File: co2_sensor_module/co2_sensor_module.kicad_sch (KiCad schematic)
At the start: 0 parts

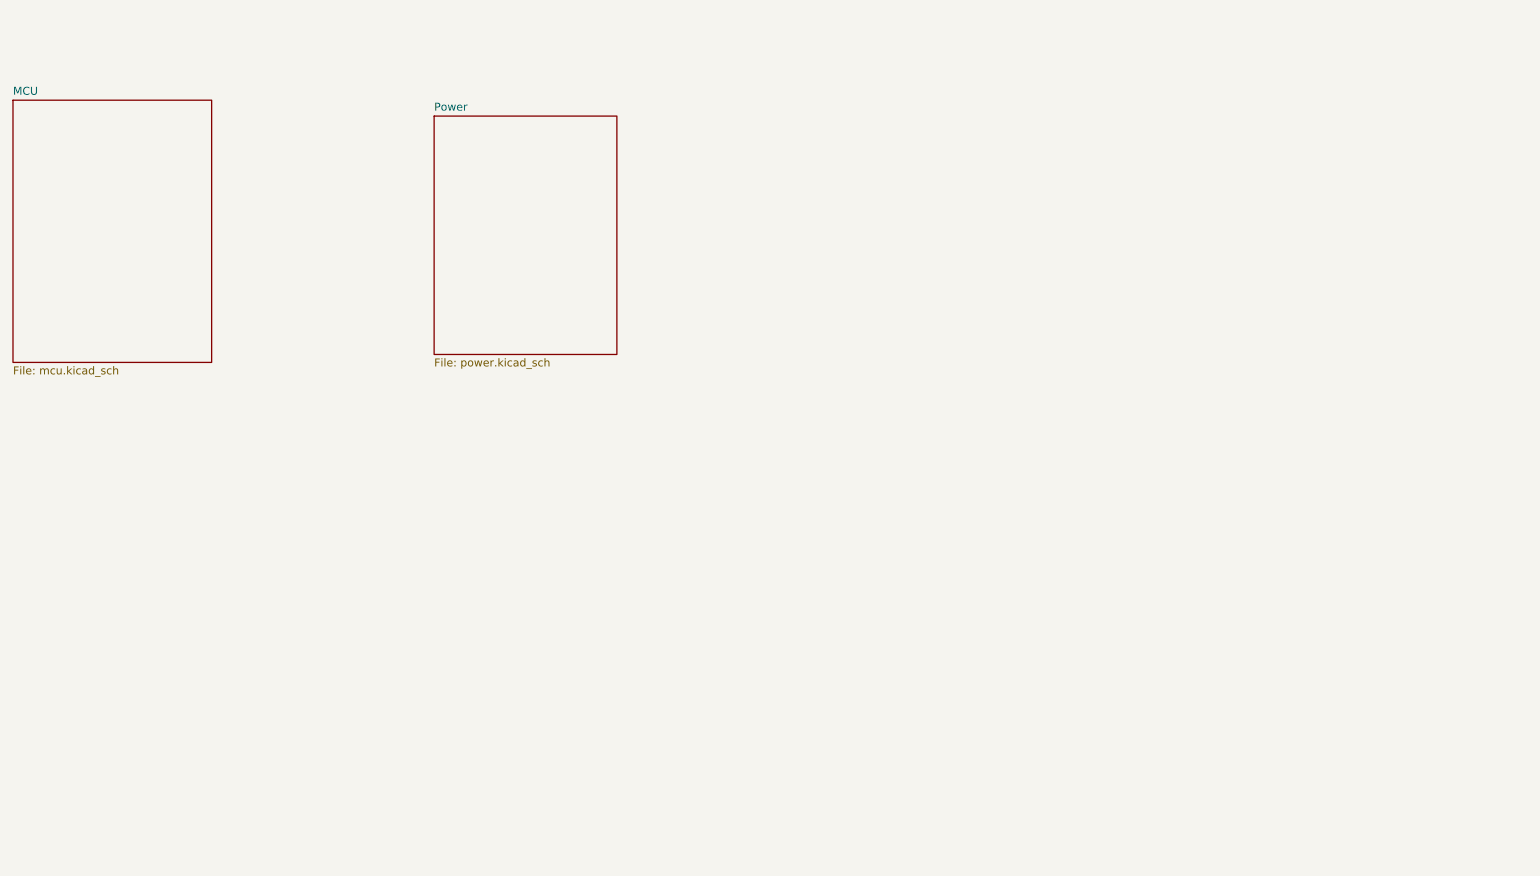
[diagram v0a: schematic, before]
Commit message: mostly done w/ sensor module
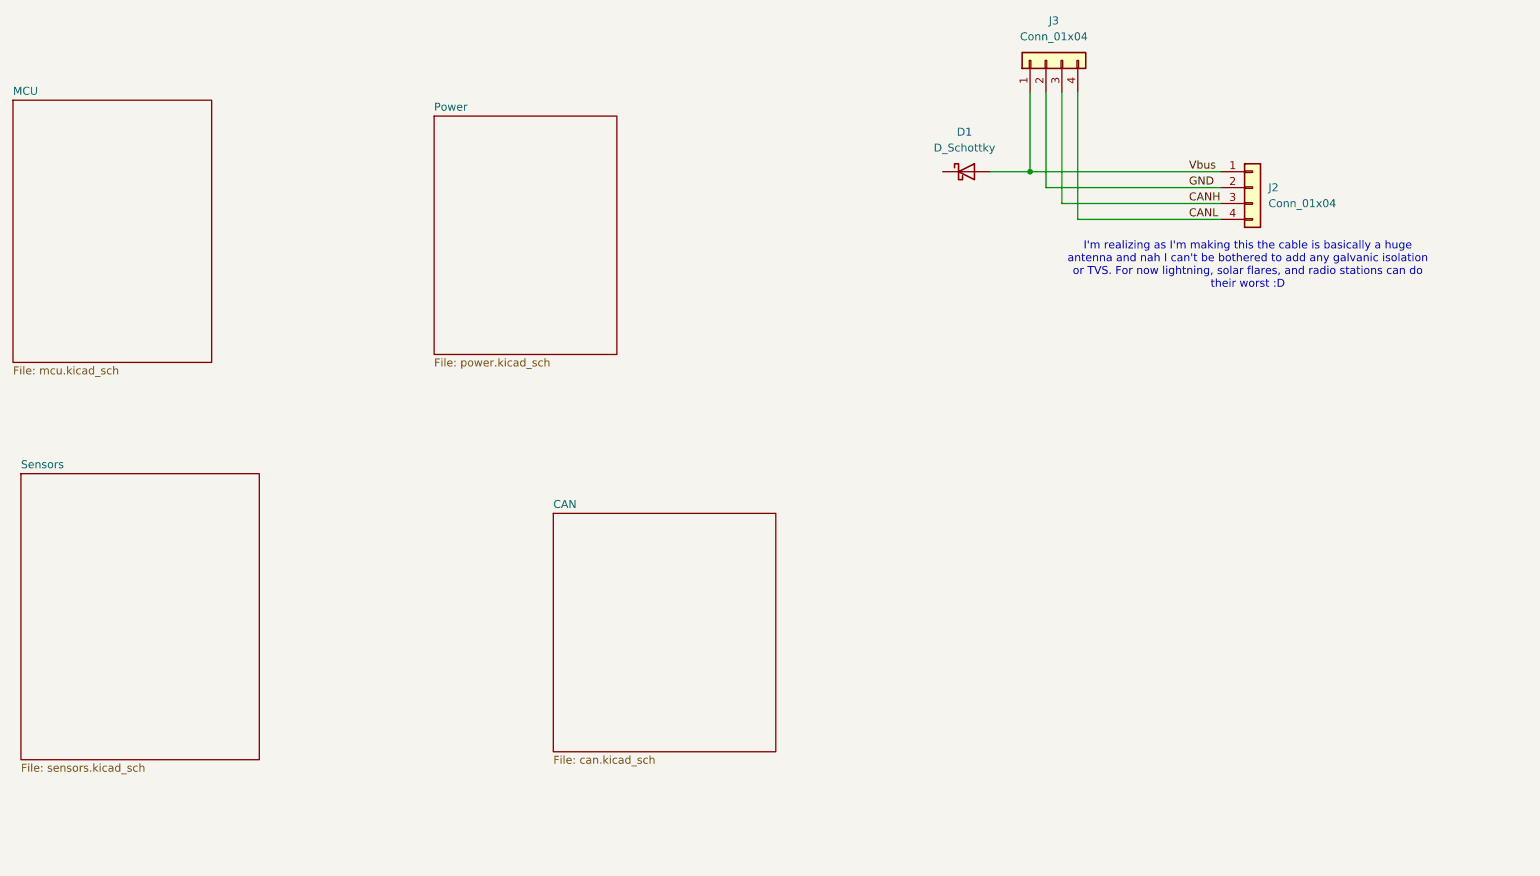
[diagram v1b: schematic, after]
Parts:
- added D1: D_Schottky, Diode_SMD:D_SOD-123, symbol Device:D_Schottky
- added J2, J3: Conn_01x04, symbol Connector_Generic:Conn_01x04
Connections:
- new net CANH: J2.3 (Pin_3), J3.3 (Pin_3)
- new net CANL: J2.4 (Pin_4), J3.4 (Pin_4)
- new net GND: J2.2 (Pin_2), J3.2 (Pin_2)
- new net Vbus: D1.2 (A), J2.1 (Pin_1), J3.1 (Pin_1)
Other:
- added sheet CAN (can.kicad_sch)
- added sheet Sensors (sensors.kicad_sch)
- note added: "I'm realizing as I'm making this the cable is basically a huge antenna and nah I can't be bothered to add any galvanic isolation or TVS. For now lightning, solar flares, and radio stations can do their worst :D"

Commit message: first draft of sensor schematic is done!
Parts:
- added J4: Conn_01x03, symbol Connector_Generic:Conn_01x03
- added J5: Conn_01x04, symbol Connector_Generic:Conn_01x04
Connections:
- net GND: now also J4.1 (Pin_1), J5.1 (Pin_1)
- net Power/Vbus: now reaches D1.1 (K)
- new net MCU/I2C_SCL: J5.4 (Pin_4)
- new net MCU/I2C_SDA: J5.3 (Pin_3)
- new net MCU/UART_RX: J4.2 (Pin_2)
- new net MCU/UART_TX: J4.3 (Pin_3)
- new net P3V3: J5.2 (Pin_2)
- no-connect marks 0 -> 1
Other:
- sheet CAN ports: added CANH, CANL, GND, P3V3, PV50, RX, STANDBY, TX; removed none
- sheet MCU ports: added CAN_RX, CAN_STANDBY, CAN_TX, GND, I2C_SCL, I2C_SDA, P3V3, UART_RX, UART_TX, ~{nRST}; removed none
- sheet Power ports: added GND, P3V3, P3V3_PGOOD, P5V0, P5V0_PGOOD, Vbus; removed none
- sheet Sensors ports: added GND, I2C_SCL, I2C_SDA, P3V3; removed none
- note added: "A UART header"
- note added: "An I2C expansion header"
- note added: "At least some reverse voltage protection would be useful"

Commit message: added wip hub + o2 sensor
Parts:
- J2, J3: footprint (none) -> Connector_JST:JST_PH_B4B-PH-K_1x04_P2.00mm_Vertical
- J4: footprint (none) -> Connector_PinHeader_2.54mm:PinHeader_1x03_P2.54mm_Vertical
- J5: footprint (none) -> Connector_PinHeader_2.54mm:PinHeader_1x04_P2.54mm_Vertical
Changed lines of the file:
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@@
 			)
 		)
-		(property "Footprint" ""
+		(property "Footprint" "Connector_PinHeader_2.54mm:PinHeader_1x04_P2.54mm_Vertical"
 			(at 106.68 140.97 0)
 			(hide yes)
@@
 			)
 		)
-		(property "Footprint" ""
+		(property "Footprint" "Connector_PinHeader_2.54mm:PinHeader_1x03_P2.54mm_Vertical"
 			(at 167.64 137.16 0)
 			(hide yes)
@@
 			)
 		)
-		(property "Footprint" ""
+		(property "Footprint" "Connector_JST:JST_PH_B4B-PH-K_1x04_P2.00mm_Vertical"
 			(at 215.9 38.1 0)
 			(hide yes)
@@
 			)
 		)
-		(property "Footprint" ""
+		(property "Footprint" "Connector_JST:JST_PH_B4B-PH-K_1x04_P2.00mm_Vertical"
 			(at 248.92 58.42 0)
 			(hide yes)

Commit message: some work on layout for co2 sensor unit
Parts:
- removed J5: Conn_01x04, Connector_PinHeader_2.54mm:PinHeader_1x04_P2.54mm_Vertical, symbol Connector_Generic:Conn_01x04
- added H1, H2, H3, H4: MountingHole 3M, MountingHole:MountingHole_3.2mm_M3, symbol Mechanical:MountingHole
- added J6, J7: Conn_01x05, Connector_PinHeader_2.54mm:PinHeader_1x05_P2.54mm_Vertical, symbol Connector_Generic:Conn_01x05
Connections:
- net GND: now also J6.1 (Pin_1), J7.1 (Pin_1)
- net MCU/I2C_SCL: now also J6.5 (Pin_5), J7.5 (Pin_5)
- net MCU/I2C_SDA: now also J6.4 (Pin_4), J7.4 (Pin_4)
- net P3V3: now also J6.2 (Pin_2), J7.2 (Pin_2)
- new net P5V0: J6.3 (Pin_3), J7.3 (Pin_3)
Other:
- note added: "Some I2C expansion headers"
- note removed: "An I2C expansion header"

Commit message: (mostly) finalized sensing units + progress on surface hub
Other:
- note removed: "I'm realizing as I'm making this the cable is basically a huge antenna and nah I can't be bothered to add any galvanic isolation or TVS. For now lightning, solar flares, and radio stations can do their worst :D"
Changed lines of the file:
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@@
-		)
-	)
-	(text "I'm realizing as I'm making this the cable is basically a huge\nantenna and nah I can't be bothered to add any galvanic isolation\nor TVS. For now lightning, solar flares, and radio stations can do\ntheir worst :D"
-		(exclude_from_sim no)
-		(at 252.984 70.358 0)
-		(effects
-			(font
-				(size 1.27 1.27)
-			)
 		)
 	)

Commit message: progress on solar charging + misc
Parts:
- D1: value D_Schottky -> B5819W Schottky
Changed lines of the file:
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@@
 			)
 		)
-		(property "Value" "D_Schottky"
+		(property "Value" "B5819W Schottky"
 			(at 202.8825 52.07 0)
 			(show_name no)
